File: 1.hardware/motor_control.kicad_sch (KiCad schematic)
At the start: 87 parts, among them IC4 UCC27712QDRQ1, IC5 UCC27712QDRQ1, IC6 UCC27712QDRQ1, J13 MOTOR_UVW, J14 MOTOR_HALL_SENSOR, Q10 STL130N6F7, Q11 STL130N6F7, Q6 STL130N6F7, Q7 STL130N6F7, Q8 STL130N6F7, Q9 STL130N6F7

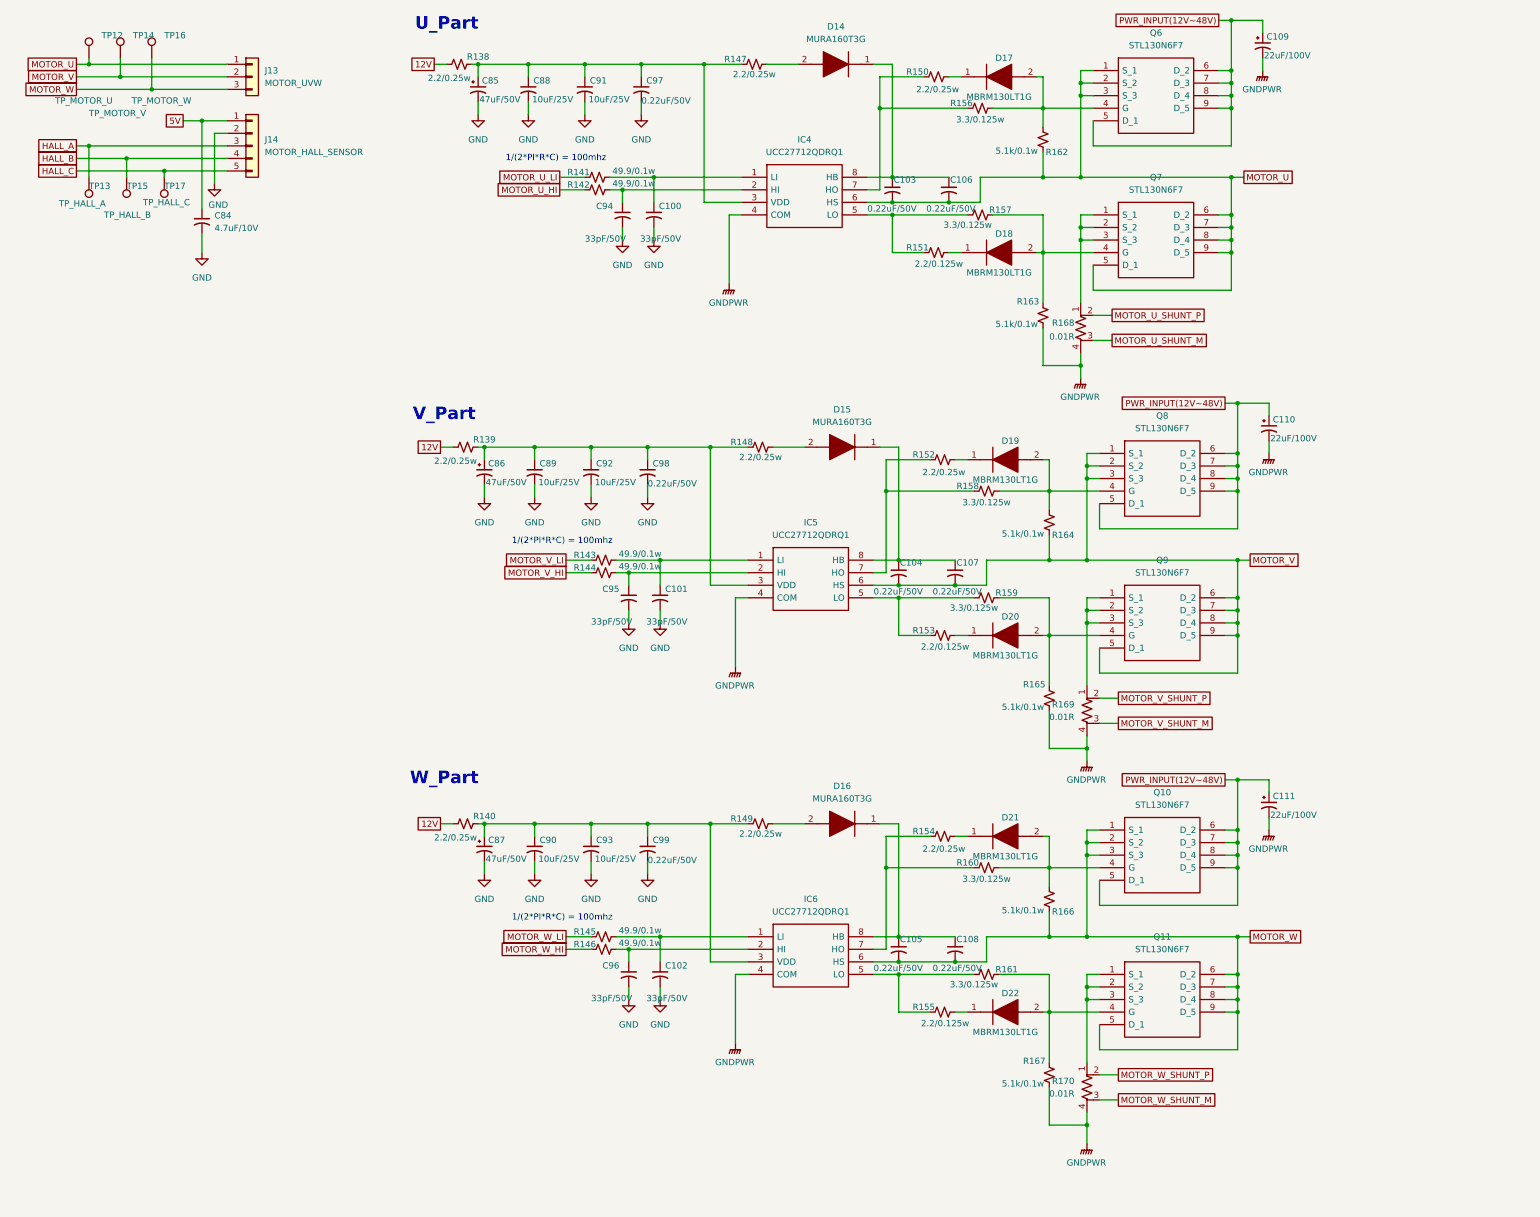
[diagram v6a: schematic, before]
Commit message: 풋프린트 연결 완료
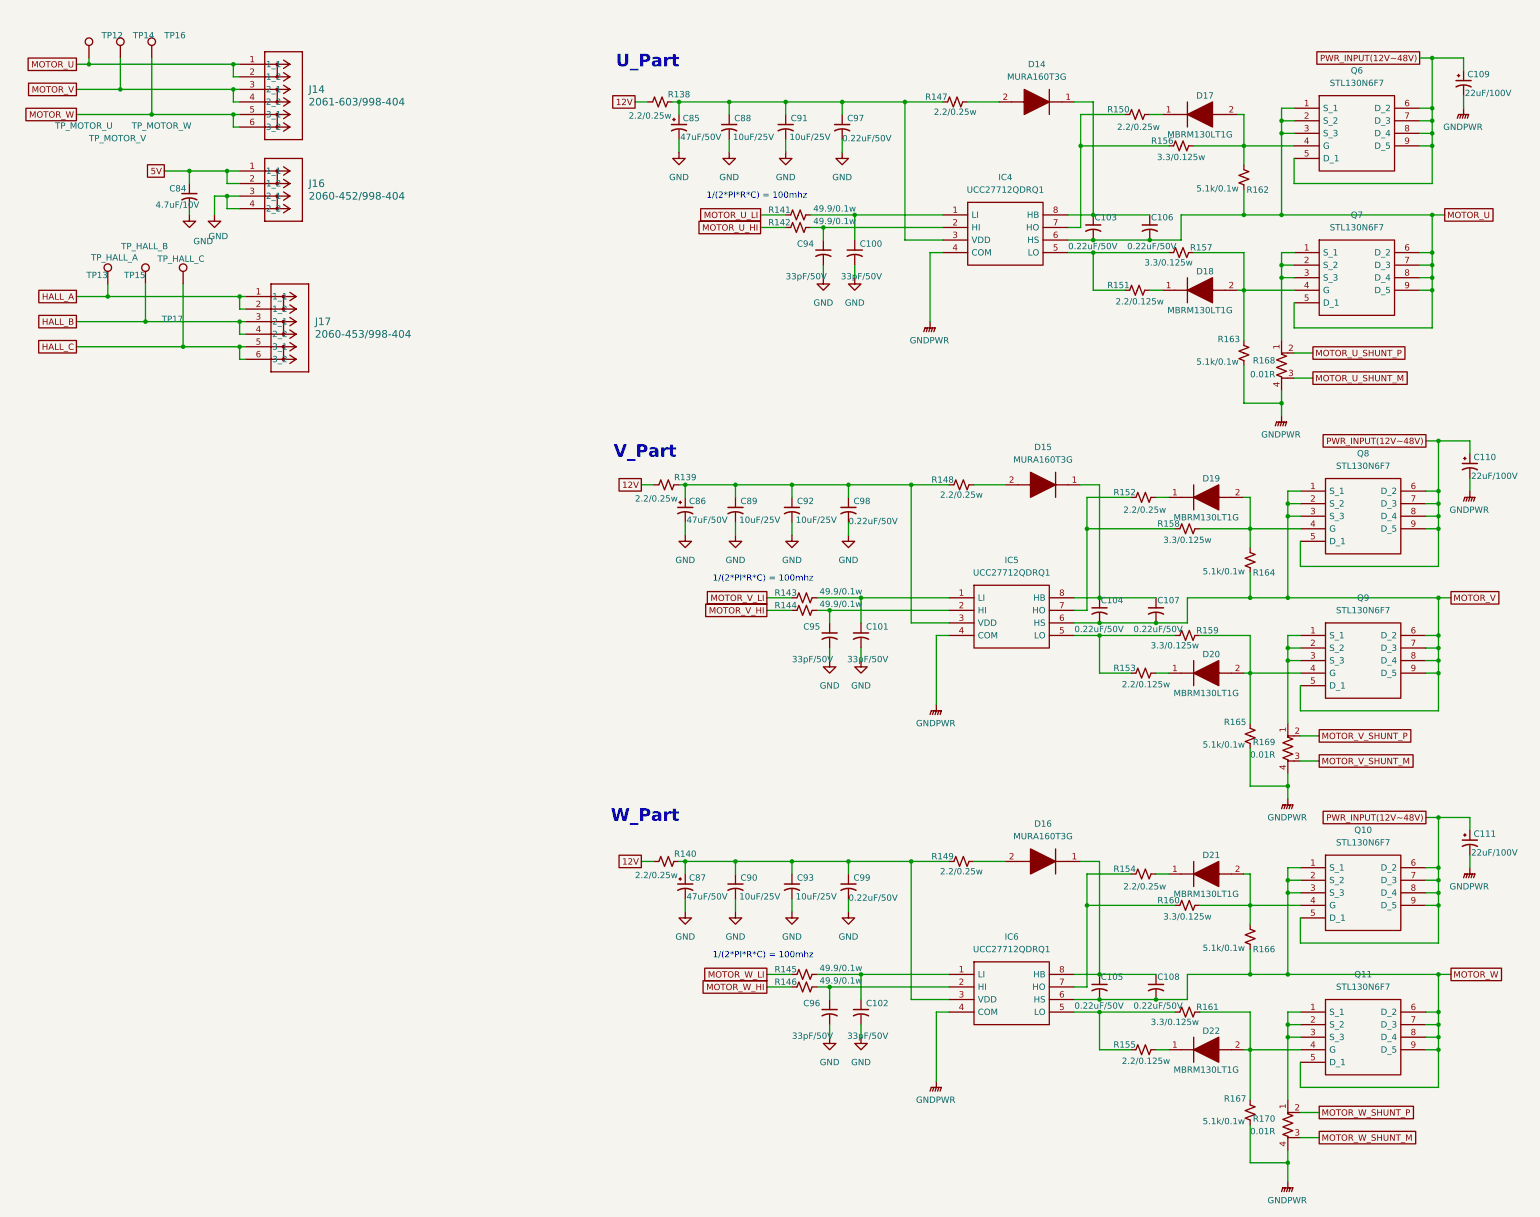
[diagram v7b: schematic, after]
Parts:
- removed J13: MOTOR_UVW, symbol Connector_Generic:Conn_01x03
- removed J14: MOTOR_HALL_SENSOR, symbol Connector_Generic:Conn_01x05
- added J14: 2061-603/998-404, ul_2061_603:CONN3_2061-603&slash_998-404_WAG, symbol 2025-12-13_07-22-42:2061-603_998-404
- added J16: 2060-452/998-404, ul_2060_452:CONN2_2060-452&slash_998-404_WAG, symbol 2025-12-13_07-20-23:2060-452_998-404
- added J17: 2060-453/998-404, ul_2060_453:CONN3_2060-453&slash_998-404_WAG, symbol 2025-12-13_07-21-44:2060-453_998-404
- D14, D15, D16: footprint DIOM5226X220N -> SamacSys_Parts_Project:DIOM5226X220N
- D17, D18, D19, D20, D21, D22: footprint MBRM130LT1G -> SamacSys_Parts_Project:MBRM130LT1G
- IC4, IC5, IC6: footprint SamacSys_Parts:SOIC127P600X175-8N -> SamacSys_Parts_Project:SOIC127P600X175-8N
- Q10, Q11, Q6, Q7, Q8, Q9: footprint SamacSys_Parts:FERD20U50DJFTR -> SamacSys_Parts_Project:FERD20U50DJFTR
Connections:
- net 5V: now also J16.1 (1_1), J16.2 (1_2)
- net GND: now also J16.3 (2_1), J16.4 (2_2)
- net HALL_A: now also J17.1 (1_1), J17.2 (1_2)
- net HALL_B: now also J17.3 (2_1), J17.4 (2_2)
- net HALL_C: now also J17.5 (3_1), J17.6 (3_2)
- net MOTOR_U: now also J14.1 (1_1), J14.2 (1_2)
- net MOTOR_V: now also J14.3 (2_1), J14.4 (2_2)
- net MOTOR_W: now also J14.5 (3_1), J14.6 (3_2)
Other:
- moved on the sheet: C100, C101, C102, C103, C104, C105, C106, C107, C108, C109, C110, C111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

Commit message: 중간 저장
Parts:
- renumbered D14 to D13, D15 to D14, D16 to D15, D17 to D16, D18 to D17, D19 to D18, D20 to D19, D21 to D20, D22 to D21, IC4 to IC3, IC5 to IC4, IC6 to IC5, J14 to J13, J16 to J14, J17 to J15, Q6 to Q1, Q7 to Q2, Q8 to Q3, Q9 to Q4, Q10 to Q5, Q11 to Q6, R138 to R123, R139 to R124, R140 to R125, R141 to R126, R142 to R127, R143 to R128, R144 to R129, R145 to R130, R146 to R131, R147 to R132, R148 to R133, R149 to R134, R150 to R135, R151 to R136, R152 to R137, R153 to R138, R154 to R139, R155 to R140, R156 to R141, R157 to R142, R158 to R143, R159 to R144, R160 to R145, R161 to R146, R162 to R147, R163 to R148, R164 to R149, R165 to R150, R166 to R151, R167 to R152, R168 to R153, R169 to R154, R170 to R155, TP12 to TP10, TP13 to TP11, TP14 to TP12, TP15 to TP13, TP16 to TP14, TP17 to TP15
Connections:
- net 5V: now also J14.3 (2_1), J14.4 (2_2); no longer J14.1 (1_1), J14.2 (1_2)
- net GND: now also J14.1 (1_1), J14.2 (1_2); no longer J14.3 (2_1), J14.4 (2_2)
- net HALL_A: now also J15.5 (3_1), J15.6 (3_2); no longer J15.1 (1_1), J15.2 (1_2)
- net HALL_C: now also J15.1 (1_1), J15.2 (1_2); no longer J15.5 (3_1), J15.6 (3_2)
- net MOTOR_U: now also J13.5 (3_1), J13.6 (3_2); no longer J13.1 (1_1), J13.2 (1_2)
- net MOTOR_W: now also J13.1 (1_1), J13.2 (1_2); no longer J13.5 (3_1), J13.6 (3_2)
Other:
- moved on the sheet: J15
